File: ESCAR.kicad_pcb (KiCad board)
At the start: 2 copper layers, 31.6 x 63.6 mm, 56 parts, among them P1 MICRO_SD, P2 BREADBOARD, P3 PROGRAM, P4 MOTOR_B, P5 MOTOR_A, P6 CONN_01X10, P7 CONN_01X10, P8 POWER_IN, P9 UNIVERSAL_PAD, SW1 RESET, SW2 MULTIFUNCTION_SW, SW3 POWER_SW, U1 ESP-WROOM-02, U2 TC117HS, U3 TC117HS, U4 LD1117CV33

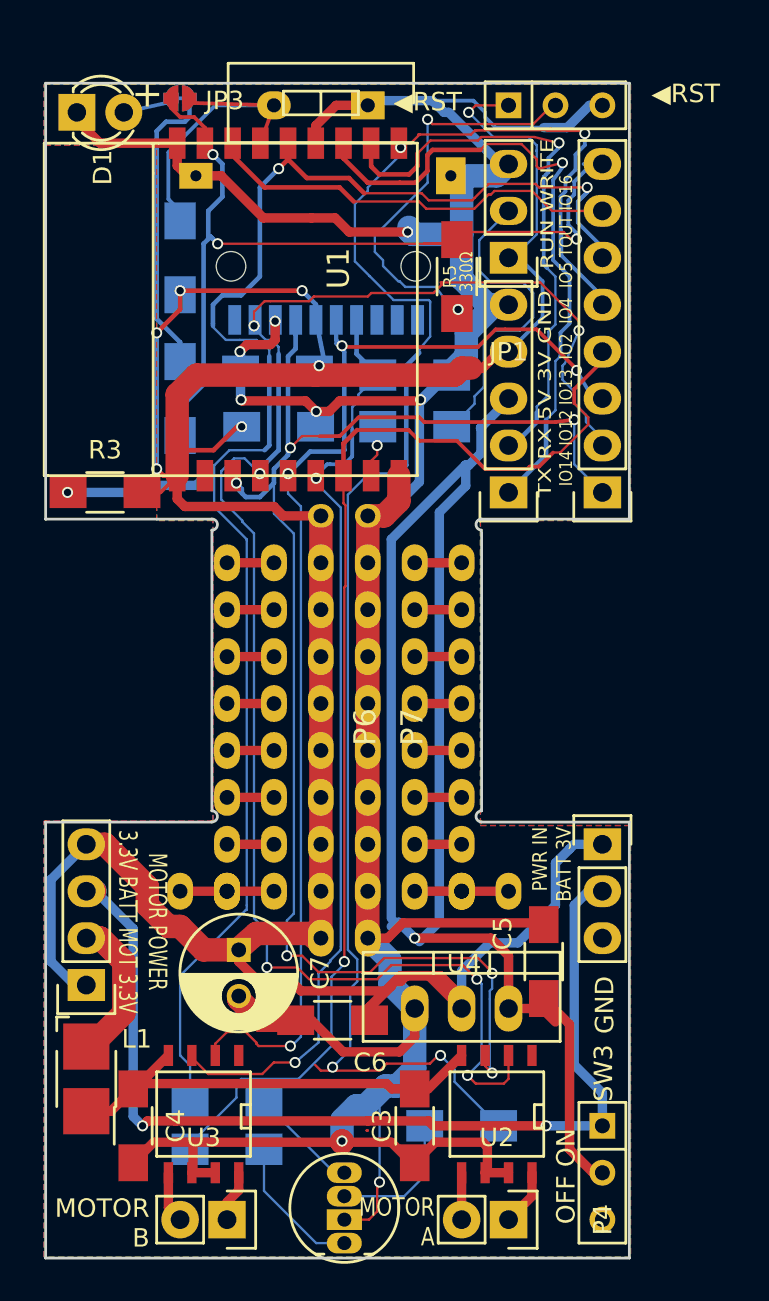
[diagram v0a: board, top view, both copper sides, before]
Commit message: add dividing resisters for RX pin , and organized many point.
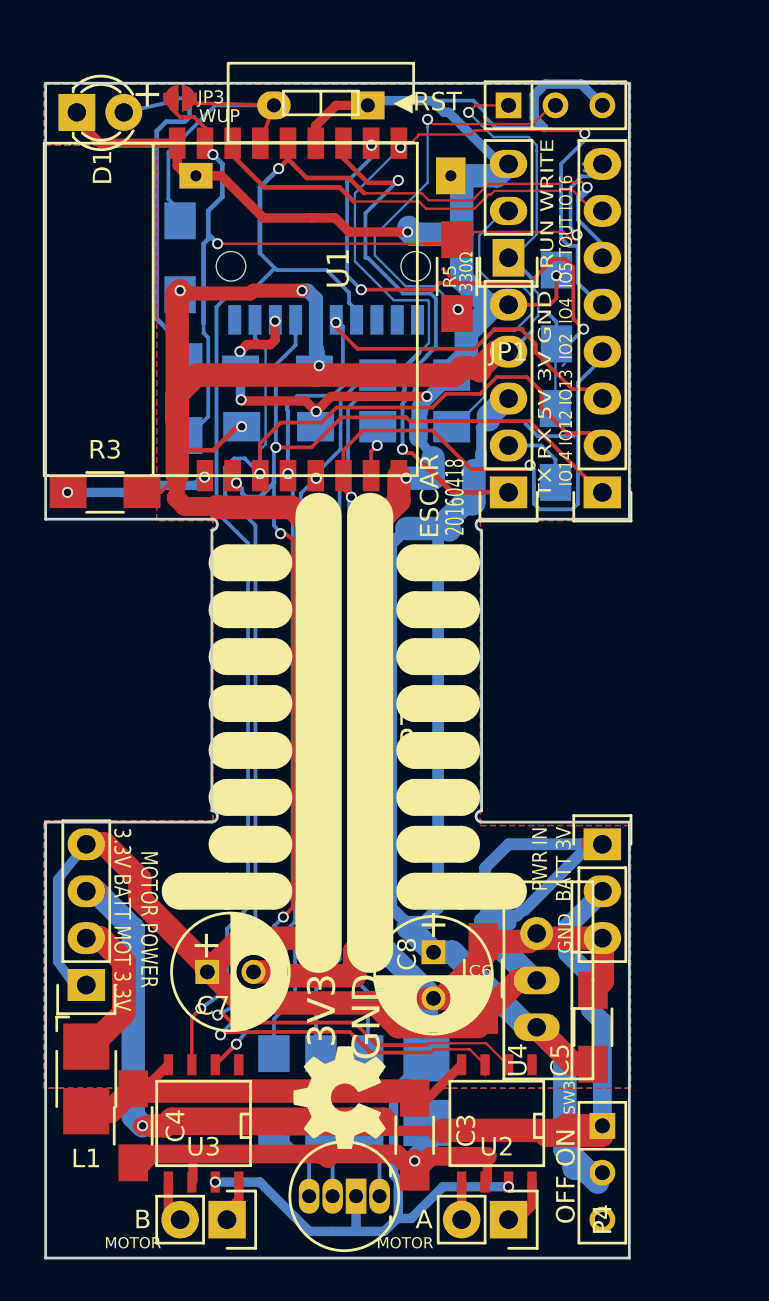
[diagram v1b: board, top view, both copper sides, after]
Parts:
- added C8: 100uF, Capacitors_ThroughHole:C_Radial_D6.3_L11.2_P2.5, F.Cu at (120.4, 98.6)
- added L2: INDUCTOR_SMALL, Inductors:Inductor_1212, B.Cu at (120.0, 106.0)
- added OSHW: 1.1, library:OSHW_LOGL_SYLK_5mm, F.Cu at (115.3, 106.4)
- added R10: 330Ω, Resistors_SMD:R_1206_HandSoldering, B.Cu at (127.1, 63.6)
- added R11: 330Ω, Resistors_SMD:R_1206_HandSoldering, B.Cu at (127.0, 71.1)
- P4: value MOTOR_B -> MOTOR_A
- P5: value MOTOR_A -> MOTOR_B
- moved C6 8.46 mm to (123.1, 100.0), turned to 90 degrees
- moved R9 8.26 mm to (116.8, 106.0), turned to 90 degrees
- moved R7 7.85 mm to (114.3, 106.0), turned to 90 degrees
- moved C5 4.45 mm to (129.0, 102.6)
- moved U4 4.34 mm to (126.0, 100.1), turned to 270 degrees
- moved D2 3.17 mm to (117.5, 111.8), turned to 270 degrees
- moved R8 2.62 mm to (111.8, 106.0), turned to 90 degrees
- moved C7 2.08 mm to (108.2, 99.6), turned to 0 degrees
- moved C3 0.51 mm to (119.4, 108.5)
- moved U2 0.51 mm to (123.8, 107.8)
- moved U3 0.51 mm to (108.0, 107.8)
- moved R6 0.36 mm to (107.0, 68.6)
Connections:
- C3 pad 2: GND -> Net-(C3-Pad2)
- C4 pad 2: GND -> Net-(C3-Pad2)
- P1 pad : GND -> (no net)
- P2 pad 6: Net-(P2-Pad6) -> Net-(P1-Pad2)
- R1 pad 2: Net-(P1-Pad2) -> Net-(R1-Pad2)
- R3 pad 2: +3V3 -> Net-(R3-Pad2)
- R8 pad 2: Net-(P2-Pad6) -> Net-(R1-Pad2)
- U1 pad 11: Net-(P3-Pad2) -> Net-(R10-Pad2)
- U1 pad 14: Net-(P2-Pad6) -> Net-(P1-Pad2)
- U1 pad 6: Net-(P1-Pad2) -> Net-(R1-Pad2)
- U2 pad 6: GND -> Net-(C3-Pad2)
- U3 pad 6: GND -> Net-(C3-Pad2)
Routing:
- net Net-(P2-Pad6): track 85.8 -> 0.00 mm, vias 2 -> 0
- net Net-(C3-Pad2): track 0.00 -> 44.5 mm, vias 0 -> 1
- net Net-(R1-Pad2): track 0.00 -> 41.2 mm, vias 0 -> 1
- net Net-(R10-Pad2): track 0.00 -> 34.1 mm, vias 0 -> 3
- net +3V3: track 169.5 -> 203.5 mm, vias 7 -> 5
- net Net-(P1-Pad2): track 51.2 -> 84.4 mm, vias 2 -> 3
- net +BATT: track 55.4 -> 86.3 mm, vias 3 -> 2
- net Net-(P3-Pad2): track 31.1 -> 4.89 mm, vias 1 -> 0
- net Net-(P2-Pad5): track 94.4 -> 79.4 mm, vias 4 -> 2
- net Net-(P1-Pad7): track 90.4 -> 85.1 mm, vias 6 -> 2
- net +5V: track 86.3 -> 90.5 mm, vias 1 -> 0
- net Net-(D2-Pad1): track 7.77 -> 3.98 mm
- net Net-(D2-Pad3): track 7.98 -> 4.61 mm
- net Net-(P2-Pad4): track 65.0 -> 61.9 mm, vias 1 -> 2
- net GND: track 195.4 -> 192.9 mm, vias 8 -> 10
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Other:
- board text added: "20160418"
- board text added: "3V3 GND"
- board text added: "A"
- board text added: "B"
- board text added: "ESCAR"
- board text added: "GND IO16 3.3V"
- board text added: "MOTOR"
- board text added: "Micro_SD:CS=IO5"
- board text added: "WUP"
- board text added: "YELLOW_LED"
- board text removed: "MOTOR A"
- board text removed: "MOTOR B"

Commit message: Ver20160517 Release. Add USB switch function, change GPIO assign.
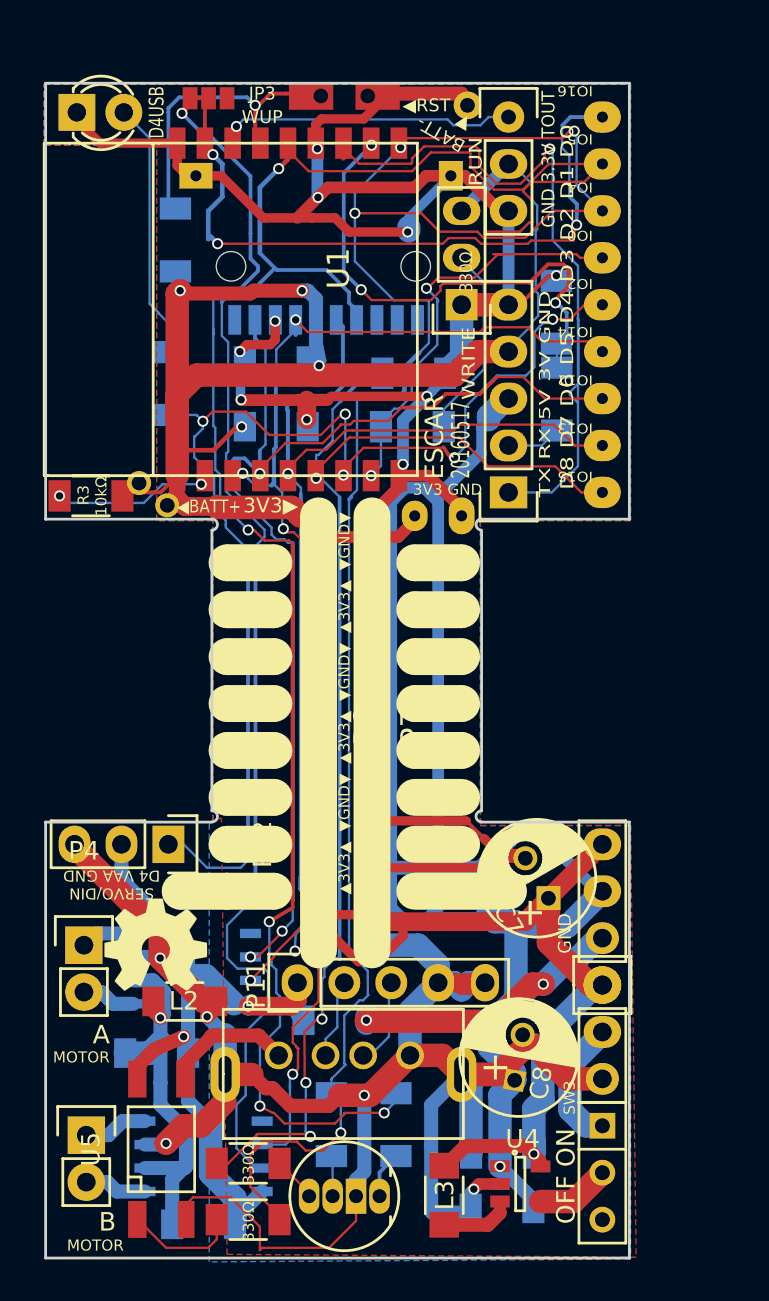
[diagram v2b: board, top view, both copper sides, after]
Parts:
- removed JP3: YELLOW_LED, library:Soldar_Jumper_Unconnected
- removed R5: 330Ω, Resistors_SMD:R_1206_HandSoldering
- removed SW2: MULTIFUNCTION_SW, Buttons_Switches_ThroughHole:SW_Micro_SPST
- added L3: 4.7uH, library:C_1206_HandSoldering_Small, F.Cu at (121.0, 111.7)
- added P10: USB_A, library:USB_A_Vertical_Short, F.Cu at (112.0, 104.1)
- added P11: USB_B, Pin_Headers:Pin_Header_Straight_1x05, F.Cu at (113.0, 100.2)
- added P12: SERVO/INPUT, Pin_Headers:Pin_Header_Straight_1x03, F.Cu at (106.0, 92.7)
- added P13: ANALOG, Pin_Headers:Pin_Header_Straight_1x03, F.Cu at (124.5, 53.3)
- added P14: BATTERY3.3V, Wire_Pads:SolderWirePad_single_0-8mmDrill, F.Cu at (106.0, 74.9)
- added P14: BATTERY3.3V, Wire_Pads:SolderWirePad_single_0-8mmDrill, F.Cu at (104.1, 73.0)
- added P15: BATTERYGND, Wire_Pads:SolderWirePad_single_0-8mmDrill, F.Cu at (121.9, 52.1)
- added P16: BREADBOARD_POWER, library:Padmatrix-wide-02x01, F.Cu at (120.7, 74.9)
- added R12: 330Ω, library:R_1206_HandSoldering_Small, F.Cu at (110.4, 113.0)
- added U5: TLP222A, Opto-Devices:Optocoupler_SMD_HandSoldering_KPC357_LTV35x_PC357_SingleChannel, F.Cu at (105.7, 109.2)
- C1, C2: footprint Capacitors_SMD:C_1206_HandSoldering -> library:C_1206_HandSoldering_Small
- C3, C4: footprint Capacitors_SMD:C_1206_HandSoldering -> library:C_1206_HandSoldering_Small; moved to B.Cu
- C5, C6: value 0.1uF -> 10uF; footprint Capacitors_SMD:C_1206_HandSoldering -> library:C_1206_HandSoldering_Small; moved to B.Cu
- JP1: value WRITE -> MODE_JP
- JP2: value WAKEUP_JUMPER -> WAKEUP; footprint library:Soldar_Jumper_Unconnected -> library:Solder_Jumper_3
- L1: footprint Inductors:Inductor_1212 -> library:C_1206_HandSoldering_Small; moved to B.Cu
- L2: footprint Inductors:Inductor_1212 -> library:C_1206_HandSoldering_Small; moved to F.Cu
- P2: footprint Pin_Headers:Pin_Header_Straight_1x08 -> library:SolderWirePad_Oval_9xInline_0-6mmDrill
- P9: value UNIVERSAL_PAD -> UNIVERSAL PAD
- R1, R10, R11, R2, R3, R4, R6, R7, R9: footprint Resistors_SMD:R_1206_HandSoldering -> library:R_1206_HandSoldering_Small
- R8: footprint Resistors_SMD:R_1206_HandSoldering -> library:R_1206_HandSoldering_Small; moved to F.Cu
- SW1: footprint Buttons_Switches_ThroughHole:SW_DIP_x1_Slide -> library:SW_SMD_3x6_WithHole
- U2, U3: moved to B.Cu
- U4: value LD1117CV33 -> MT5201-3.3N; footprint TO_SOT_Packages_THT:TO-220_Neutral123_Vertical -> TO_SOT_Packages_SMD:SOT-23-5
- moved JP4 27.9 mm to (129.5, 100.3)
- moved P4 27.4 mm to (101.5, 98.2), turned to 0 degrees
- moved C7 18.9 mm to (126.6, 95.6), turned to 120 degrees
- moved U2 18.5 mm to (107.3, 99.4), turned to 270 degrees
- moved C3 14.7 mm to (105.4, 104.0), turned to 180 degrees
- moved L2 13.9 mm to (106.9, 101.2), turned to 0 degrees
- moved L1 13.8 mm to (115.1, 102.2), turned to 180 degrees
- moved OSHW 13.0 mm to (105.4, 98.1), turned to 0 degrees
- moved U4 11.1 mm to (125.1, 111.1), turned to 0 degrees
- moved C5 11.0 mm to (124.1, 112.4), turned to 180 degrees
- moved P2 10.2 mm to (129.5, 63.5), turned to 270 degrees
- moved C6 9.56 mm to (124.1, 109.5), turned to 180 degrees
- moved P5 8.89 mm to (101.6, 108.5), turned to 0 degrees
- moved C8 8.21 mm to (124.8, 105.5), turned to 80 degrees
- moved P8 7.62 mm to (129.5, 100.3)
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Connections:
- JP1 pad 1: +3V3 -> GND
- JP1 pad 3: GND -> +3V3
- JP4 pad 3: +BATT -> +5V
- P1 pad : (no net) -> GND
- P2 pad 1: Net-(P1-Pad5) -> Net-(JP2-Pad2)
- P2 pad 2: Net-(P1-Pad7) -> Net-(P1-Pad2)
- P2 pad 3: Net-(P1-Pad3) -> Net-(P2-Pad3)
- P2 pad 5: Net-(P2-Pad5) -> Net-(P12-Pad1)
- P2 pad 6: Net-(P1-Pad2) -> Net-(P1-Pad5)
- P2 pad 7: Net-(P2-Pad7) -> Net-(P1-Pad7)
- P2 pad 8: Net-(JP2-Pad2) -> Net-(P1-Pad3)
- R1 pad 2: Net-(R1-Pad2) -> Net-(P2-Pad9)
- R2 pad 1: Net-(R2-Pad1) -> Net-(JP1-Pad2)
- R2 pad 2: Net-(JP1-Pad2) -> Net-(P2-Pad4)
- R3 pad 2: Net-(R3-Pad2) -> +3V3
- R6 pad 1: Net-(JP3-Pad1) -> Net-(D1-Pad2)
- R6 pad 2: Net-(JP2-Pad2) -> Net-(P12-Pad1)
- R7 pad 2: Net-(P2-Pad5) -> Net-(P2-Pad3)
- R8 pad 2: Net-(R1-Pad2) -> Net-(P2-Pad9)
- R9 pad 2: Net-(P2-Pad4) -> Net-(JP2-Pad2)
- U1 pad 10: Net-(P2-Pad5) -> Net-(P2-Pad3)
- U1 pad 16: Net-(P2-Pad7) -> Net-(P13-Pad1)
- U1 pad 6: Net-(R1-Pad2) -> Net-(P2-Pad9)
- U1 pad 7: Net-(P2-Pad4) -> Net-(P12-Pad1)
- U1 pad 8: Net-(R2-Pad1) -> Net-(P2-Pad4)
- U4 pad 1: GND -> +5V
- U4 pad 2: +3V3 -> GND
- U4 pad 3: +5V -> Net-(L3-Pad1)
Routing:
- net Net-(P2-Pad3): track 0.00 -> 101.8 mm, vias 0 -> 4
- net Net-(P2-Pad5): track 79.4 -> 0.00 mm, vias 2 -> 0
- net +BATT: track 86.3 -> 7.05 mm, vias 2 -> 0
- net Net-(P2-Pad9): track 0.00 -> 71.2 mm, vias 0 -> 4
- net Net-(P12-Pad1): track 0.00 -> 66.7 mm, vias 0 -> 5
- net GND: track 192.9 -> 255.9 mm, vias 10 -> 16
- net Net-(JP2-Pad2): track 56.4 -> 113.3 mm, vias 3 -> 8
- net Net-(R1-Pad2): track 41.2 -> 0.00 mm, vias 1 -> 0
- net Net-(P2-Pad4): track 61.9 -> 23.9 mm
- net Net-(C3-Pad2): track 44.5 -> 20.8 mm
- net Net-(P1-Pad5): track 82.9 -> 59.8 mm, vias 5 -> 4
- net Net-(P2-Pad7): track 22.8 -> 0.00 mm
- net Net-(R5-Pad1): track 22.3 -> 0.00 mm, vias 2 -> 0
- net +5V: track 90.5 -> 112.6 mm, vias 0 -> 1
- net +3V3: track 203.5 -> 181.9 mm
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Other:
- board text added: "20160517"
- board text added: "3.3V VAA 5V"
- board text added: "3V BATT GND"
- board text added: "3V3▶"
- board text added: "BATT- ▼"
- board text added: "D0:IO16 D1:IO5 D2:IO4 D3:IO0 D4:IO2 D5:IO14 D6:IO12 D7:IO13 D8:IO15 D9:RX D10:TX"
- board text added: "D4USB"
- board text added: "D8 D7 D6 D5 D4 D3 D2 D1 D0"
- board text added: "GND 3.3V TOUT"
- board text added: "IO15 IO13 IO12 IO14 IO2 IO0 IO4 IO5 IO16"
- board text added: "MicroSD:CS=D2 USB=D4 R=D16 G=D2 B=D15"
- board text added: "RUN"
- board text added: "SERVO/DIN D4 VAA GND"
- board text added: "WRITE"
- board text added: "←POWER CONFIG"
- board text added: "▲3V3▲ ▼GND▼ ▲3V3▲ ▼GND▼ ▲3V3▲ ▼GND▼"
- board text added: "◀BATT+"
- board text added: "◀POWER IN"
- board text removed: "20160418"
- board text removed: "GND IO16 3.3V"
- board text removed: "IO14 IO12 IO13 IO2 IO4 IO5 TOUT IO16"
- board text removed: "JP2"
- board text removed: "MOTOR POWER 3.3V BATT MOT 3.3V"
- board text removed: "Micro_SD:CS=IO5"
- board text removed: "PWR IN BATT 3V"
- board text removed: "RUN WRITE"
- board text removed: "YELLOW_LED"
- board text removed: "◀SW_IN"

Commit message: Ver20160617 Release. change PORT mapping, pin header hole size, silk. and few bug fix
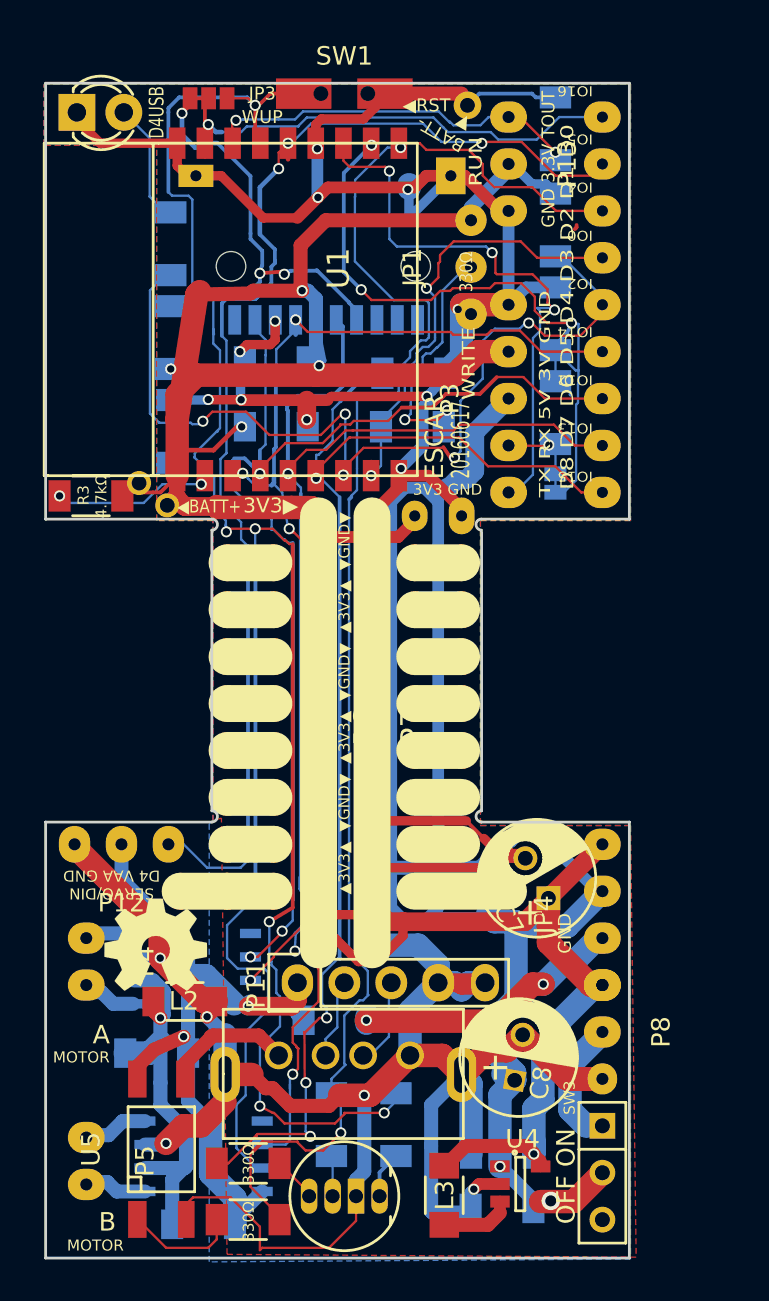
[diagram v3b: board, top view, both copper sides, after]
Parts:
- added C9: 0.1uF, library:C_1206_HandSoldering_Small, B.Cu at (106.2, 70.4)
- added JP3: JUMPER, library:Solder_Jumper_2, B.Cu at (127.0, 73.2)
- added R13: 4.7kΩ, library:R_1206_HandSoldering_Small, B.Cu at (127.0, 54.0)
- added R5: 4.7kΩ, library:R_1206_HandSoldering_Small, B.Cu at (127.0, 59.2)
- JP1, P12, P13, P8: footprint Pin_Headers:Pin_Header_Straight_1x03 -> library:SolderWirePad_Oval_3xInline_0-65mmDrill
- JP4: footprint Pin_Headers:Pin_Header_Straight_1x04 -> library:SolderWirePad_Oval_4xInline_0-65mmDrill
- P3: footprint Pin_Headers:Pin_Header_Straight_1x05 -> library:SolderWirePad_Oval_5xInline_0-65mmDrill
- P4, P5: footprint Pin_Headers:Pin_Header_Straight_1x02 -> library:SolderWirePad_Oval_2xInline_0-65mmDrill
- R1, R2, R3, R4: value 10kΩ -> 4.7kΩ
- moved R6 7.57 mm to (106.2, 60.2)
- moved R4 5.29 mm to (106.2, 65.3)
- moved P3 5.08 mm to (124.5, 68.6), turned to 90 degrees
- moved JP4 3.81 mm to (129.5, 96.5), turned to 90 degrees
- moved P12 2.54 mm to (103.5, 92.7), turned to 180 degrees
- moved P8 2.54 mm to (129.5, 102.9), turned to 270 degrees
- moved P13 2.54 mm to (124.5, 55.9), turned to 270 degrees
- moved JP1 2.09 mm to (122.4, 61.5), turned to 90 degrees
- moved P5 1.40 mm to (101.6, 109.9), turned to 270 degrees
- moved P4 0.90 mm to (101.6, 99.1), turned to 270 degrees
- moved R11 0.74 mm to (127.0, 69.3)
- moved R10 0.36 mm to (127.0, 64.3)
- moved SW1 0.13 mm to (115.6, 52.1)
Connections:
- P1 pad : GND -> (no net)
- P1 pad 2: Net-(P1-Pad2) -> Net-(JP2-Pad2)
- P2 pad 2: Net-(P1-Pad2) -> Net-(P12-Pad1)
- P2 pad 5: Net-(P12-Pad1) -> Net-(P2-Pad5)
- P3 pad 2: Net-(P3-Pad2) -> Net-(JP3-Pad1)
- R10 pad 2: Net-(R10-Pad2) -> Net-(JP3-Pad1)
- R11 pad 1: Net-(P3-Pad2) -> Net-(JP3-Pad1)
- R11 pad 2: Net-(R10-Pad2) -> Net-(JP3-Pad1)
- R6 pad 2: Net-(P12-Pad1) -> Net-(P2-Pad5)
- U1 pad 11: Net-(R10-Pad2) -> Net-(JP3-Pad1)
- U1 pad 14: Net-(P1-Pad2) -> Net-(P12-Pad1)
- U1 pad 7: Net-(P12-Pad1) -> Net-(P2-Pad5)
- U3 pad 3: Net-(P1-Pad2) -> Net-(JP2-Pad2)
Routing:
- net Net-(P1-Pad2): track 99.3 -> 0.00 mm, vias 1 -> 0
- net Net-(P2-Pad5): track 0.00 -> 51.2 mm, vias 0 -> 5
- net Net-(JP3-Pad1): track 0.00 -> 43.9 mm, vias 0 -> 4
- net Net-(JP2-Pad2): track 113.3 -> 151.3 mm, vias 8 -> 9
- net Net-(R10-Pad2): track 28.3 -> 0.00 mm, vias 3 -> 0
- net Net-(P2-Pad3): track 101.8 -> 85.8 mm, vias 4 -> 2
- net Net-(P3-Pad1): track 43.1 -> 31.4 mm, vias 1 -> 3
- net Net-(JP2-Pad1): track 16.5 -> 25.2 mm
- net Net-(D1-Pad2): track 14.0 -> 6.64 mm
- net Net-(P13-Pad1): track 17.0 -> 21.4 mm, vias 1 -> 2
- net GND: track 255.9 -> 259.7 mm
- net Net-(JP1-Pad2): track 11.4 -> 14.8 mm, vias 0 -> 2
- net +3V3: track 181.9 -> 185.3 mm
- net Net-(P3-Pad2): track 2.95 -> 0.00 mm
- net +5V: track 112.6 -> 115.3 mm, vias 1 -> 2
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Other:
- rule trace_min: 0.127 -> 0.0762
- rule via_min_drill: 0.3 -> 0.127
- rule via_min_size: 0.4 -> 0.254
- board text added: "20160617"
- board text added: "3.3V 5V VAA"
- board text removed: "20160517"
- board text removed: "3.3V VAA 5V"
